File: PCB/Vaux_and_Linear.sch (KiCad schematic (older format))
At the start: 32 parts, among them U14 AP65211AWU-7, U2 TS462CDT, U3 AZ1084CD-3.3

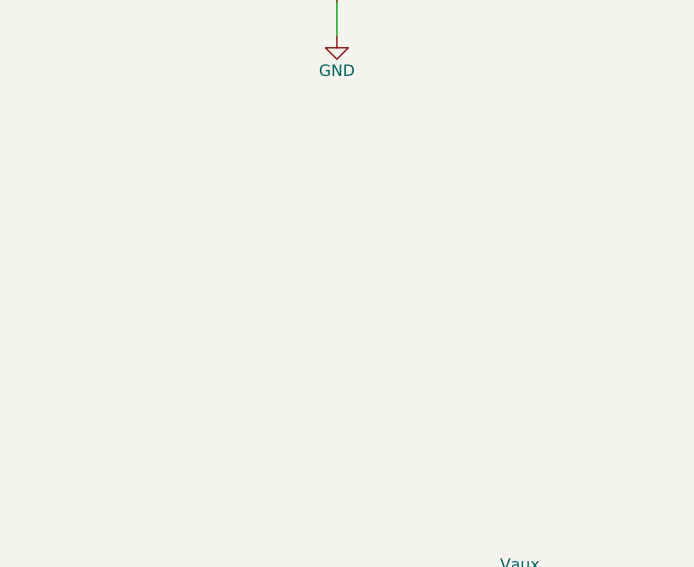
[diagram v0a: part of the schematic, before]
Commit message: Added R142, updated layout
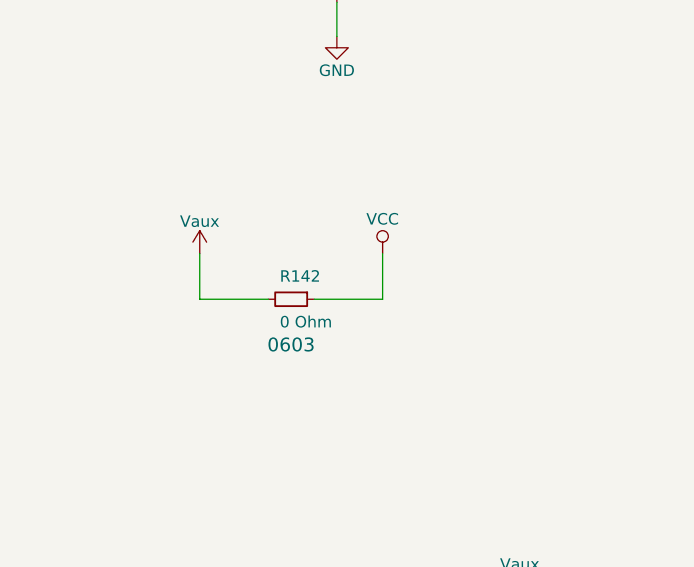
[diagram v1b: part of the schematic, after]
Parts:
- added R142: 0 Ohm, Resistors_SMD:R_0603, symbol R_Small
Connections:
- net VCC: now also R142.1
- net Vaux: now also R142.2
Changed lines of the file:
@@
 Wire Wire Line
 	3200 4700 3200 4900
+$Comp
+L Vaux #PWR041
+U 1 1 5BF0F8C3
+P 1800 3200
+F 0 "#PWR041" H 1800 3050 50  0001 C CNN
+F 1 "Vaux" H 1800 3340 50  0000 C CNN
+F 2 "" H 1800 3200 50  0001 C CNN
+F 3 "" H 1800 3200 50  0001 C CNN
+	1    1800 3200
+	1    0    0    -1
+$EndComp
+Wire Wire Line
+	1800 3200 1800 3400
+$Comp
+L VCC #PWR042
+U 1 1 5BF0FA10
+P 2600 3200
+F 0 "#PWR042" H 2600 3050 50  0001 C CNN
+F 1 "VCC" H 2600 3350 50  0000 C CNN
+F 2 "" H 2600 3200 50  0001 C CNN
+F 3 "" H 2600 3200 50  0001 C CNN
+	1    2600 3200
+	1    0    0    -1
+$EndComp
+Wire Wire Line
+	2600 3200 2600 3400
+$Comp
+L R_Small R142
+U 1 1 5BF0FAF0
+P 2200 3400
+F 0 "R142" V 2100 3350 50  0000 L CNN
+F 1 "0 Ohm" V 2300 3350 50  0000 L CNN
+F 2 "Resistors_SMD:R_0603" H 2200 3400 50  0001 C CNN
+F 3 "" H 2200 3400 50  0001 C CNN
+F 4 "0603" V 2400 3400 60  0000 C CNN "Package"
+	1    2200 3400
+	0    1    1    0
+$EndComp
+Wire Wire Line
+	2600 3400 2300 3400
+Wire Wire Line
+	1800 3400 2100 3400
 $EndSCHEMATC

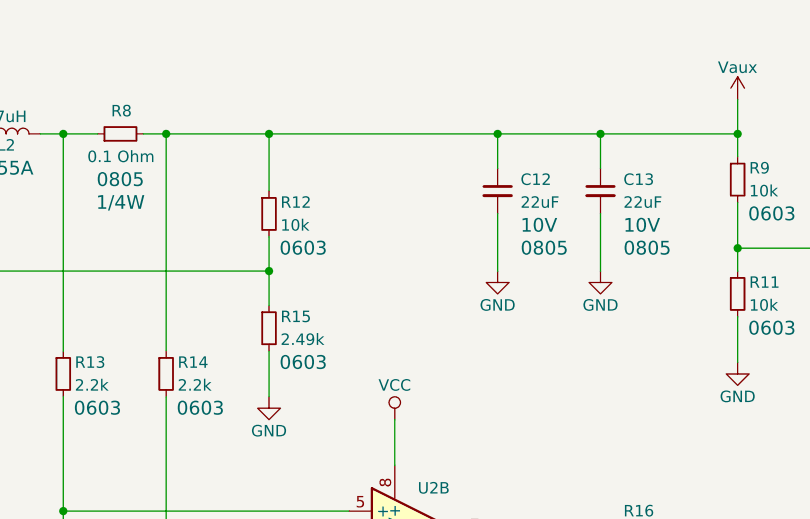
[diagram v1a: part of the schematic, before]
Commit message: Added ELOAD to sch and imported to layout
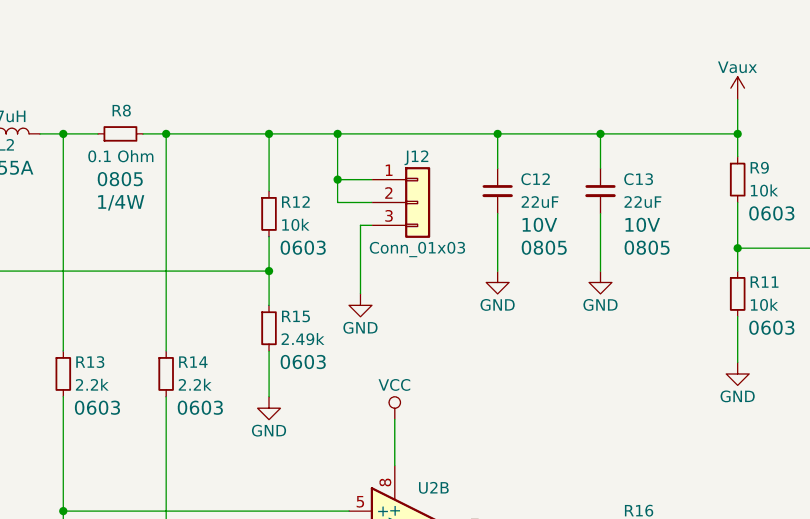
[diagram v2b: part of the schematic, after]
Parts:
- added J12: Conn_01x03, Pin_Headers:Pin_Header_Straight_1x03_Pitch2.54mm_SMD_Pin1Right, symbol Conn_01x03
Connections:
- net GND: now also J12.3 (Pin_3)
- net Vaux: now also J12.1 (Pin_1), J12.2 (Pin_2)
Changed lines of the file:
@@
 $Descr A 11000 8500
 encoding utf-8
-Sheet 3 11
+Sheet 3 12
 Title "Vaux_and_Linear"
 Date "2018-06-12"
-Rev "01"
+Rev "02"
 Comp ""
 Comment1 ""
@@
 Wire Wire Line
 	1800 3400 2100 3400
+$Comp
+L Conn_01x03 J12
+U 1 1 5BF5B69B
+P 6650 1550
+F 0 "J12" H 6650 1750 50  0000 C CNN
+F 1 "Conn_01x03" H 6650 1350 50  0000 C CNN
+F 2 "Pin_Headers:Pin_Header_Straight_1x03_Pitch2.54mm_SMD_Pin1Right" H 6650 1550 50  0001 C CNN
+F 3 "" H 6650 1550 50  0001 C CNN
+	1    6650 1550
+	1    0    0    -1
+$EndComp
+$Comp
+L GND #PWR043
+U 1 1 5BF5B772
+P 6400 1950
+F 0 "#PWR043" H 6400 1700 50  0001 C CNN
+F 1 "GND" H 6400 1800 50  0000 C CNN
+F 2 "" H 6400 1950 50  0001 C CNN
+F 3 "" H 6400 1950 50  0001 C CNN
+	1    6400 1950
+	1    0    0    -1
+$EndComp
+Wire Wire Line
+	6400 1650 6400 1950
+Wire Wire Line
+	6400 1650 6450 1650
+Wire Wire Line
+	6450 1550 6300 1550
+Wire Wire Line
+	6300 1550 6300 1250
+Connection ~ 6300 1250
+Wire Wire Line
+	6450 1450 6300 1450
+Connection ~ 6300 1450
 $EndSCHEMATC
